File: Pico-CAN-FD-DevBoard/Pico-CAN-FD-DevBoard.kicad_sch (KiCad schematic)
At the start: 51 parts, among them CN1 SM04B-SRSS-TB (LF)(SN), J1 Conn_01x03, J2 Conn_01x08, J3 USB_C_Receptacle_USB2.0_14P, SW1 SW_Push, SW2 SW_Push, U1 RP2350A, U2 MCP251863T-H-SS, U3 W25Q128JVS, U4 W25Q128JVS, U5 ESD2CAN24DBZRQ1, U6 TPS51386RJNR, Y1 ABM8-272-T3, Y2 Crystal 40MHz

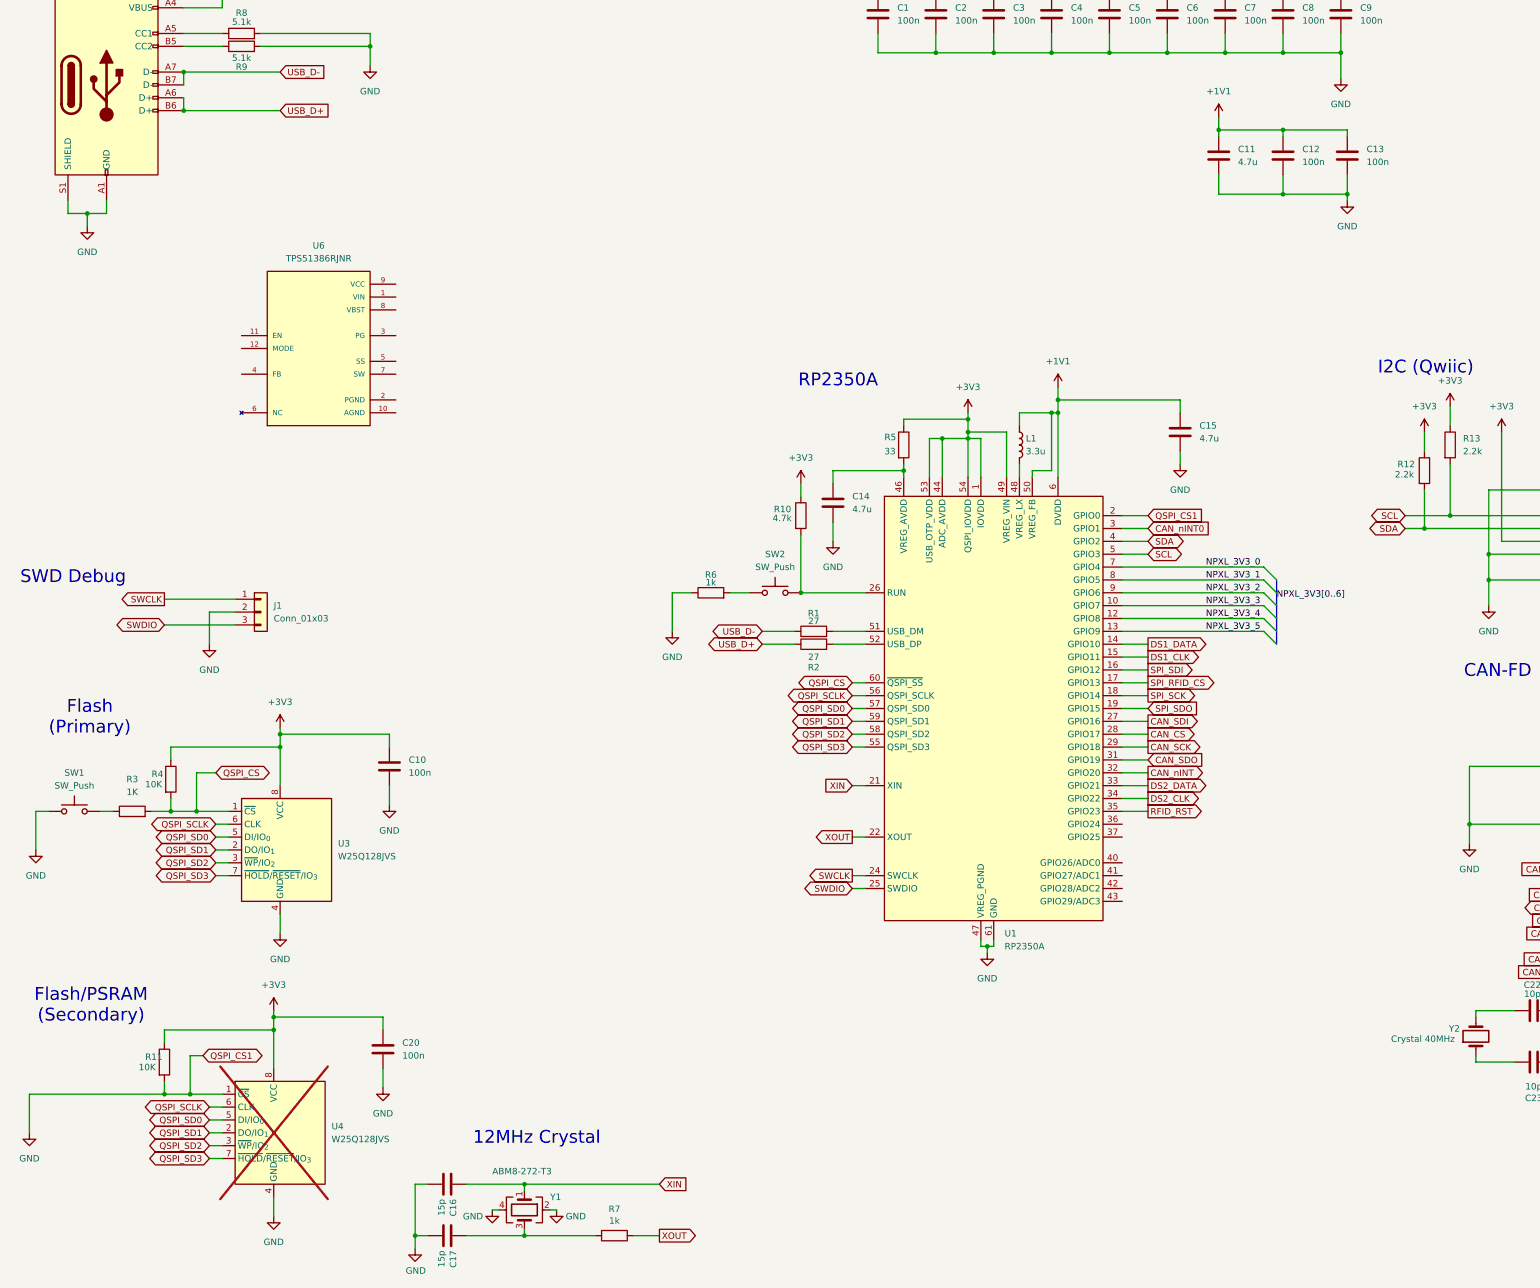
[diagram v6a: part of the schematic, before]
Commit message: rp2350b upgrade
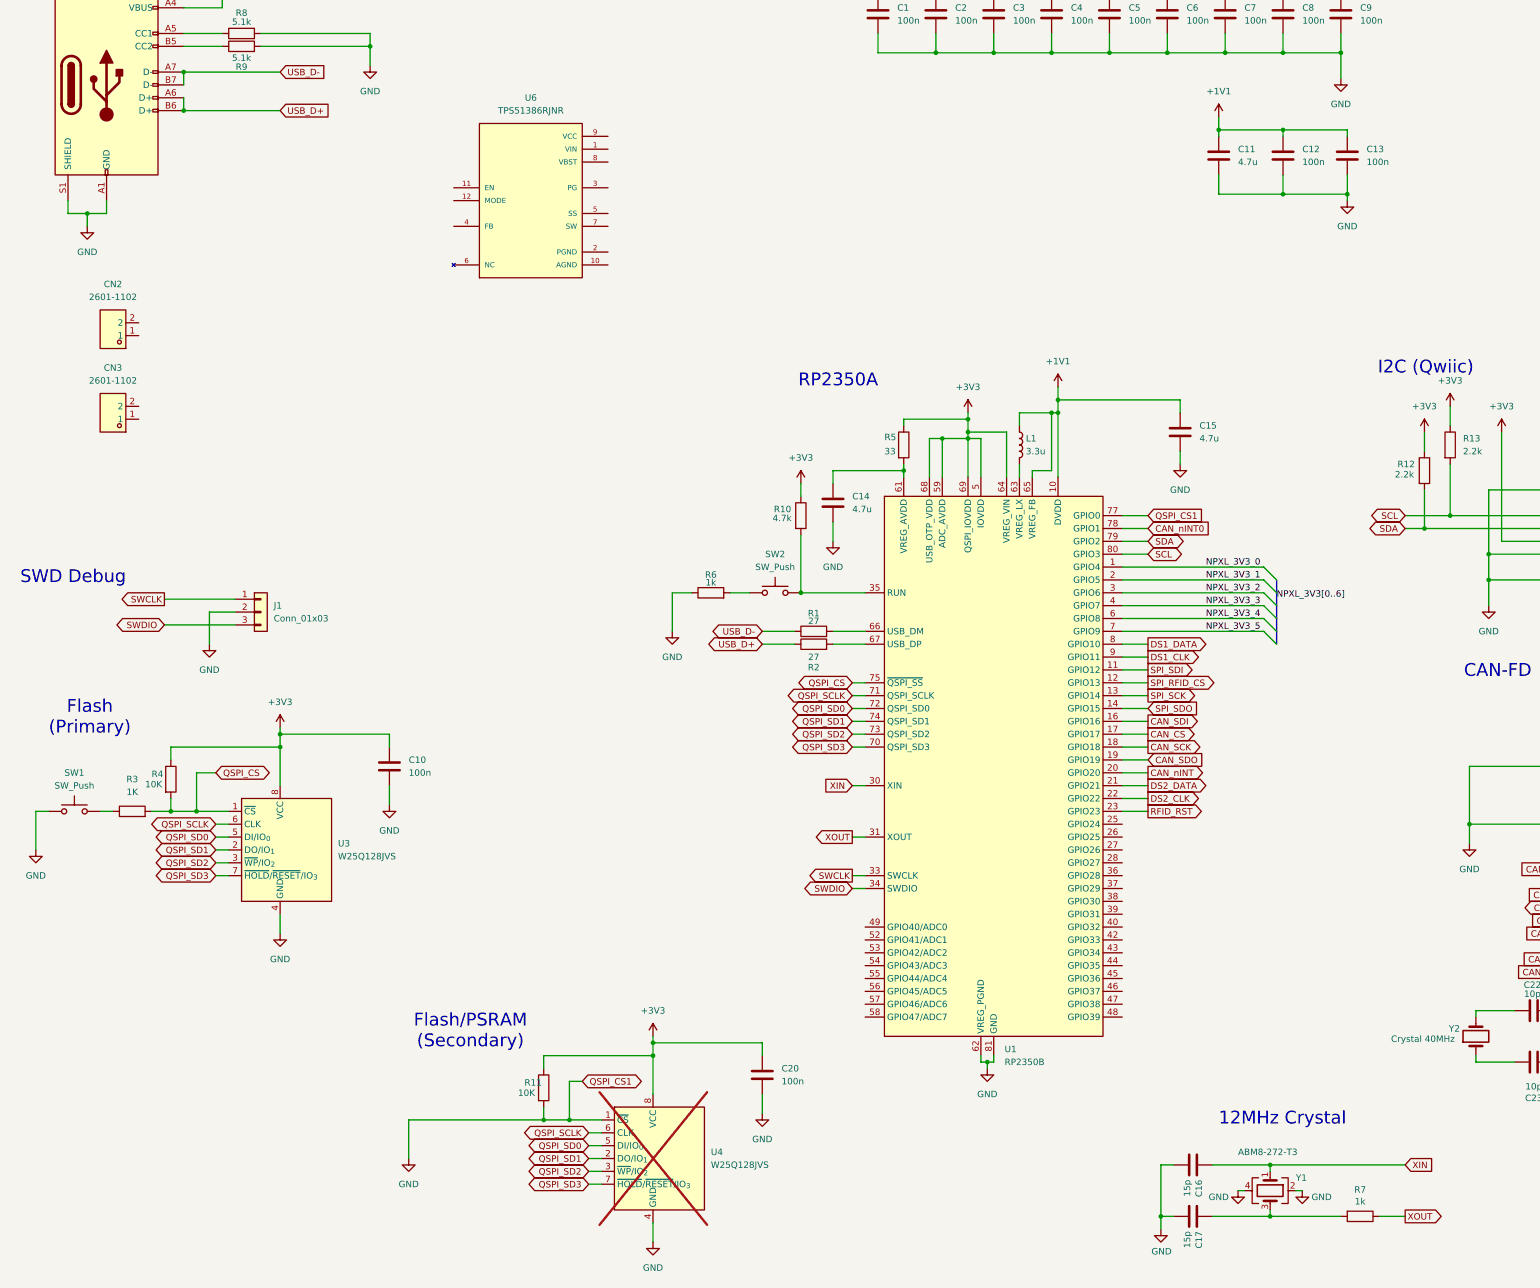
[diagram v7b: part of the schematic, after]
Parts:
- removed U1: RP2350A, Package_DFN_QFN:QFN-60-1EP_7x7mm_P0.4mm_EP3.4x3.4mm, symbol MCU_RaspberryPi:RP2350A
- added CN2: 2601-1102, easyeda2kicad:CONN-TH_6P-P3.50_2601-1103, symbol easyeda2kicad:2601-1102
- added CN3: 2601-1102, easyeda2kicad:CONN-TH_4P-P3.50_2601-1102, symbol easyeda2kicad:2601-1102
- added U1: RP2350B, Package_DFN_QFN:QFN-80-1EP_10x10mm_P0.4mm_EP3.4x3.4mm, symbol MCU_RaspberryPi:RP2350B
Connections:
- net +1V1: now also U1.10 (DVDD), U1.32 (DVDD), U1.51 (DVDD), U1.65 (VREG_FB)
- net +3V3: now also U1.15 (IOVDD), U1.24 (IOVDD), U1.29 (IOVDD), U1.41 (IOVDD), U1.5 (IOVDD), U1.50 (IOVDD), U1.59 (ADC_AVDD), U1.60 (IOVDD), U1.64 (VREG_VIN), U1.68 (USB_OTP_VDD), U1.69 (QSPI_IOVDD), U1.76 (IOVDD)
- net CAN_CS: now also U1.17 (GPIO17)
- net CAN_SCK: now also U1.18 (GPIO18)
- net CAN_SDI: now also U1.16 (GPIO16)
- net CAN_SDO: now also U1.19 (GPIO19)
- net CAN_nINT: now also U1.20 (GPIO20)
- net CAN_nINT0: now also U1.78 (GPIO1)
- net DS1_CLK: now also U1.9 (GPIO11)
- net DS1_DATA: now also U1.8 (GPIO10)
- net DS2_CLK: now also U1.22 (GPIO22)
- net DS2_DATA: now also U1.21 (GPIO21)
- net GND: now also U1.62 (VREG_PGND), U1.77 (GPIO0), U1.81 (GND)
- net NPXL_3V3_0: now also U1.1 (GPIO4)
- net NPXL_3V3_1: now also U1.2 (GPIO5)
- net NPXL_3V3_2: now also U1.3 (GPIO6)
- net NPXL_3V3_3: now also U1.4 (GPIO7)
- net NPXL_3V3_4: now also U1.6 (GPIO8)
- net NPXL_3V3_5: now also U1.7 (GPIO9)
- net QSPI_CS: now also U1.75 (~{QSPI_SS})
- net QSPI_SCLK: now also U1.71 (QSPI_SCLK)
- net QSPI_SD0: now also U1.72 (QSPI_SD0)
- net QSPI_SD1: now also U1.74 (QSPI_SD1)
- net QSPI_SD2: now also U1.73 (QSPI_SD2)
- net QSPI_SD3: now also U1.70 (QSPI_SD3)
- net RFID_RST: now also U1.23 (GPIO23)
- net SCL: now also U1.80 (GPIO3)
- net SDA: now also U1.79 (GPIO2)
- net SPI_RFID_CS: now also U1.12 (GPIO13)
- net SPI_SCK: now also U1.13 (GPIO14)
- net SPI_SDI: now also U1.11 (GPIO12)
- net SPI_SDO: now also U1.14 (GPIO15)
- net SWCLK: now also U1.33 (SWCLK)
- net SWDIO: now also U1.34 (SWDIO)
- net XIN: now also U1.30 (XIN)
- net XOUT: now also U1.31 (XOUT)
- net at C14.1, R5.2: now also U1.61 (VREG_AVDD)
- net at R2.2: now also U1.67 (USB_DP)
- net at R10.2, SW2.2: now also U1.35 (RUN)
- net at L1.2: now also U1.63 (VREG_LX)
- net at R1.2: now also U1.66 (USB_DM)
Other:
- moved on the sheet: C16, C17, C20, R11, R7, U4, U6, Y1

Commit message: fixed positions and typos
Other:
- note added: "RP2350B"
- note removed: "RP2350A"
- moved on the sheet: C10, C14, C15, C20, J1, L1, R1, R10, R11, R2, R3, R4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
